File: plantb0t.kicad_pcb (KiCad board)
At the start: 2 copper layers, 50 x 50 mm, 56 parts, among them P1 CONN_02X09, P2 USB_OTG, P3 CONN_02X03, P4 CONN_01X02, P5 CONN_01X02, P6 CONN_01X02, P7 CONN_01X02, P8 CONN_01X04, P9 CONN_01X04, Q1 BS170, Q2 BS170, SW1 SWITCH_INV, U1 ESP-12, U10 BMP280, U11 74HC(T)4051, U12 LEDx2, U2 CP2102, U3 ZXCL5213V30H5CT-ND, U4 MCP4017 100K, U5 FXL6408, U6 FC6946010R, U7 FC6946010R, U8 MCP6001, U9 PSSI2021SAY

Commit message: Starting routing from scratch
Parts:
- added P10: CONN_01X01, Connect:1pin, F.Cu at (70.0, 85.0)
- added P11: CONN_01X01, Connect:1pin, F.Cu at (70.0, 45.0)
- added P12: CONN_01X01, Connect:1pin, F.Cu at (110.0, 85.0)
- added P13: CONN_01X01, Connect:1pin, F.Cu at (110.0, 45.0)
- C1, C4, C6: footprint Capacitors_Tantalum_SMD:TantalC_SizeA_EIA-3216_HandSoldering -> Capacitors_SMD:c_elec_4x5.3
- C10, C11, C12, C13, C7, C8, C9: footprint Capacitors_SMD:C_0603 -> Capacitors_SMD:C_0805
- C2, C3, C5: footprint Capacitors_SMD:C_1206 -> Capacitors_SMD:C_0805
- SW1: footprint Buttons_Switches_ThroughHole:SW_Micro_SPST_Angled -> Buttons_Switches_SMD:SW_SPST_B3U-3100P-B
- moved C1 148.5 mm to (200.9, 104.5), turned to 0 degrees
- moved R6 143.9 mm to (220.8, 89.9)
- moved R4 142.7 mm to (215.6, 91.9), turned to 0 degrees
- moved U5 141.4 mm to (195.5, 150.6)
- moved R8 138.7 mm to (206.1, 109.1), turned to 0 degrees
- moved D1 138.6 mm to (211.6, 95.2), turned to 0 degrees
- moved R10 134.6 mm to (205.3, 138.6), turned to 0 degrees
- moved U8 133.4 mm to (207.3, 126.1)
- moved Q2 130.8 mm to (195.9, 136.5)
- moved D4 130.5 mm to (197.8, 98.6), turned to 0 degrees
- moved C7 124.8 mm to (205.9, 132.6)
- moved U11 123.9 mm to (198.4, 127.1), turned to 0 degrees
- moved Q1 122.6 mm to (192.8, 98.6), turned to 0 degrees
- moved C5 118.5 mm to (190.9, 114.9)
- moved P7 111.4 mm to (188.3, 128.6), turned to 0 degrees
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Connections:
- net /Sensor Mounts/GPIO_1 renamed /GPIO_1
- net /Sensor Mounts/I2C_CLOCK renamed /I2C_CLOCK
- net /Sensor Mounts/I2C_DATA renamed /I2C_DATA
- net /Sensor Mounts/SENSE_WIRE renamed /SENSORS
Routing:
- net /I2C_DATA: track 78.5 -> 0.00 mm, vias 1 -> 0
- net /I2C_CLOCK: track 61.0 -> 0.00 mm, vias 1 -> 0
- net +3V3: track 54.1 -> 0.00 mm, vias 1 -> 0
- net /PERM_3V3: track 88.3 -> 35.5 mm, vias 1 -> 0
- net /ESP_RESET: track 50.9 -> 9.99 mm
- net /GPIO_2: track 40.1 -> 0.00 mm
- net /GPIO_3: track 38.6 -> 0.00 mm
- net /GPIO_4: track 37.3 -> 0.00 mm
- net /CH_PD: track 40.8 -> 10.1 mm
- net /GPIO_6: track 20.8 -> 0.00 mm
- net /GPIO_5: track 20.4 -> 0.00 mm
- net /SLEEP_CTRL: track 19.9 -> 0.00 mm, vias 1 -> 0
- net /GPIO_7: track 18.4 -> 0.00 mm
- net /FLASH_TX: track 41.3 -> 56.7 mm, vias 1 -> 0
- net +5V: track 49.3 -> 60.8 mm, vias 3 -> 0
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
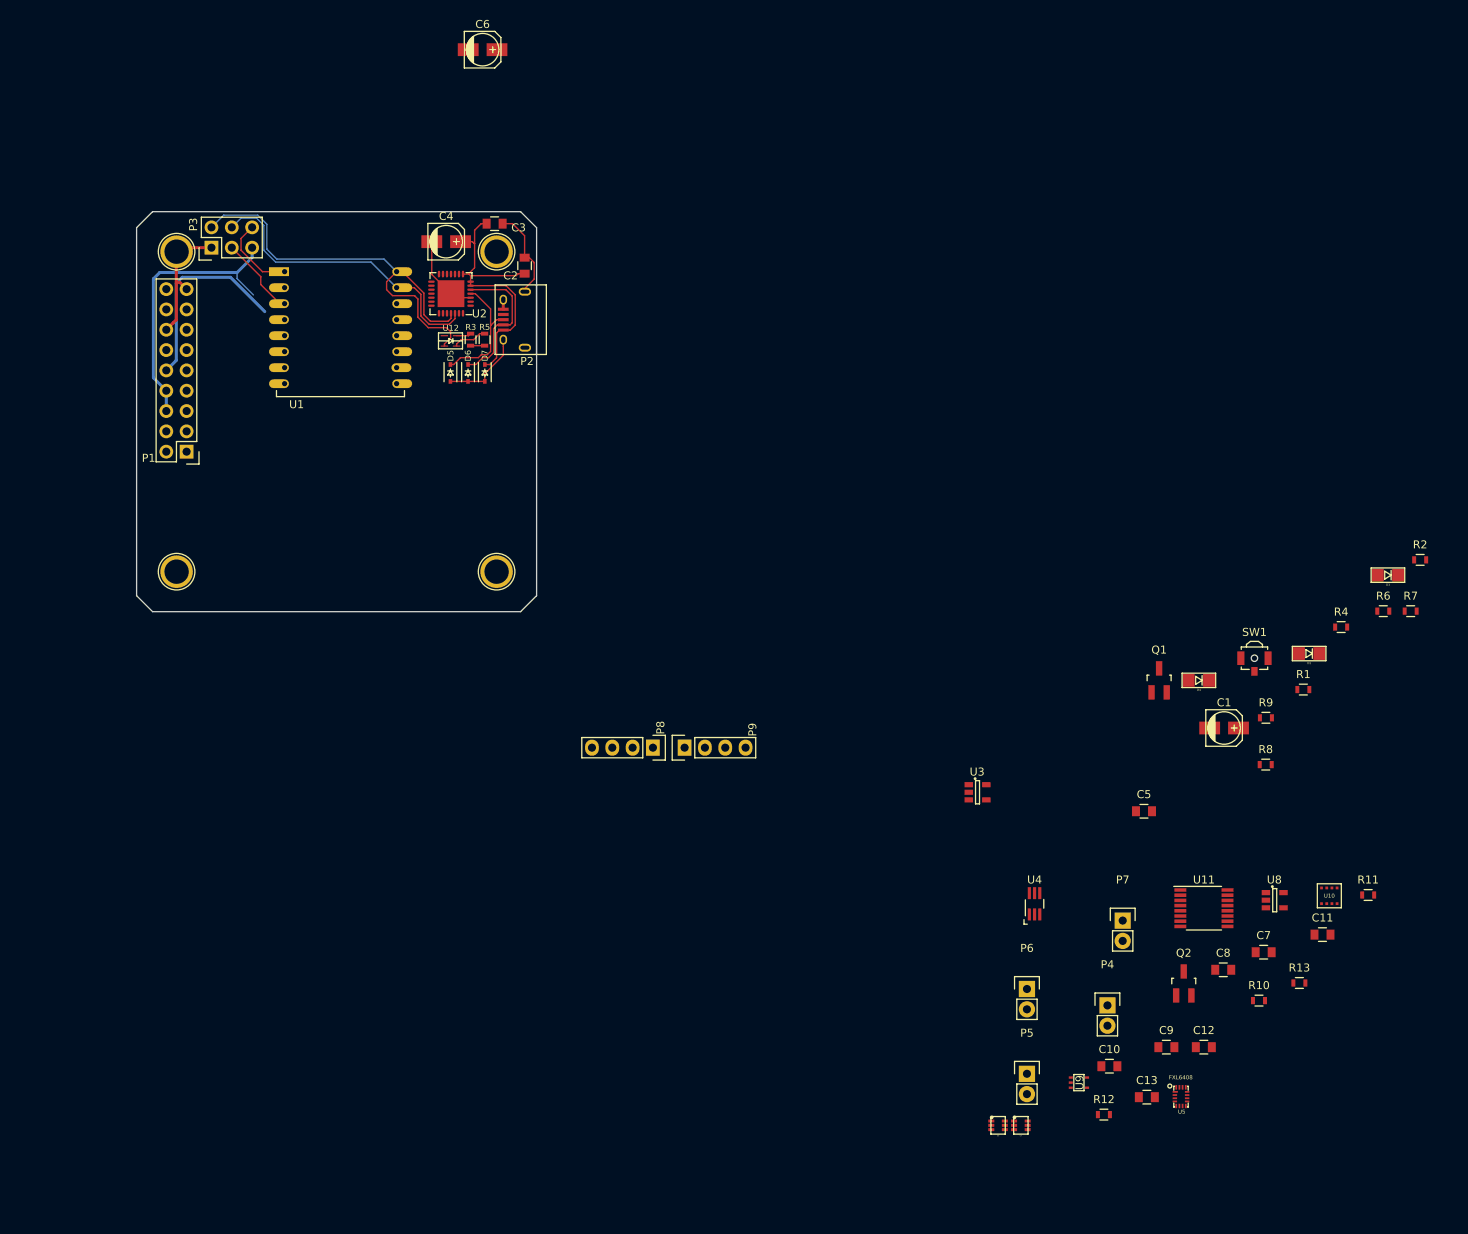
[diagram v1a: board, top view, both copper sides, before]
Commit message: Fiddling with the 5V plane for decoupling around the USB programmer
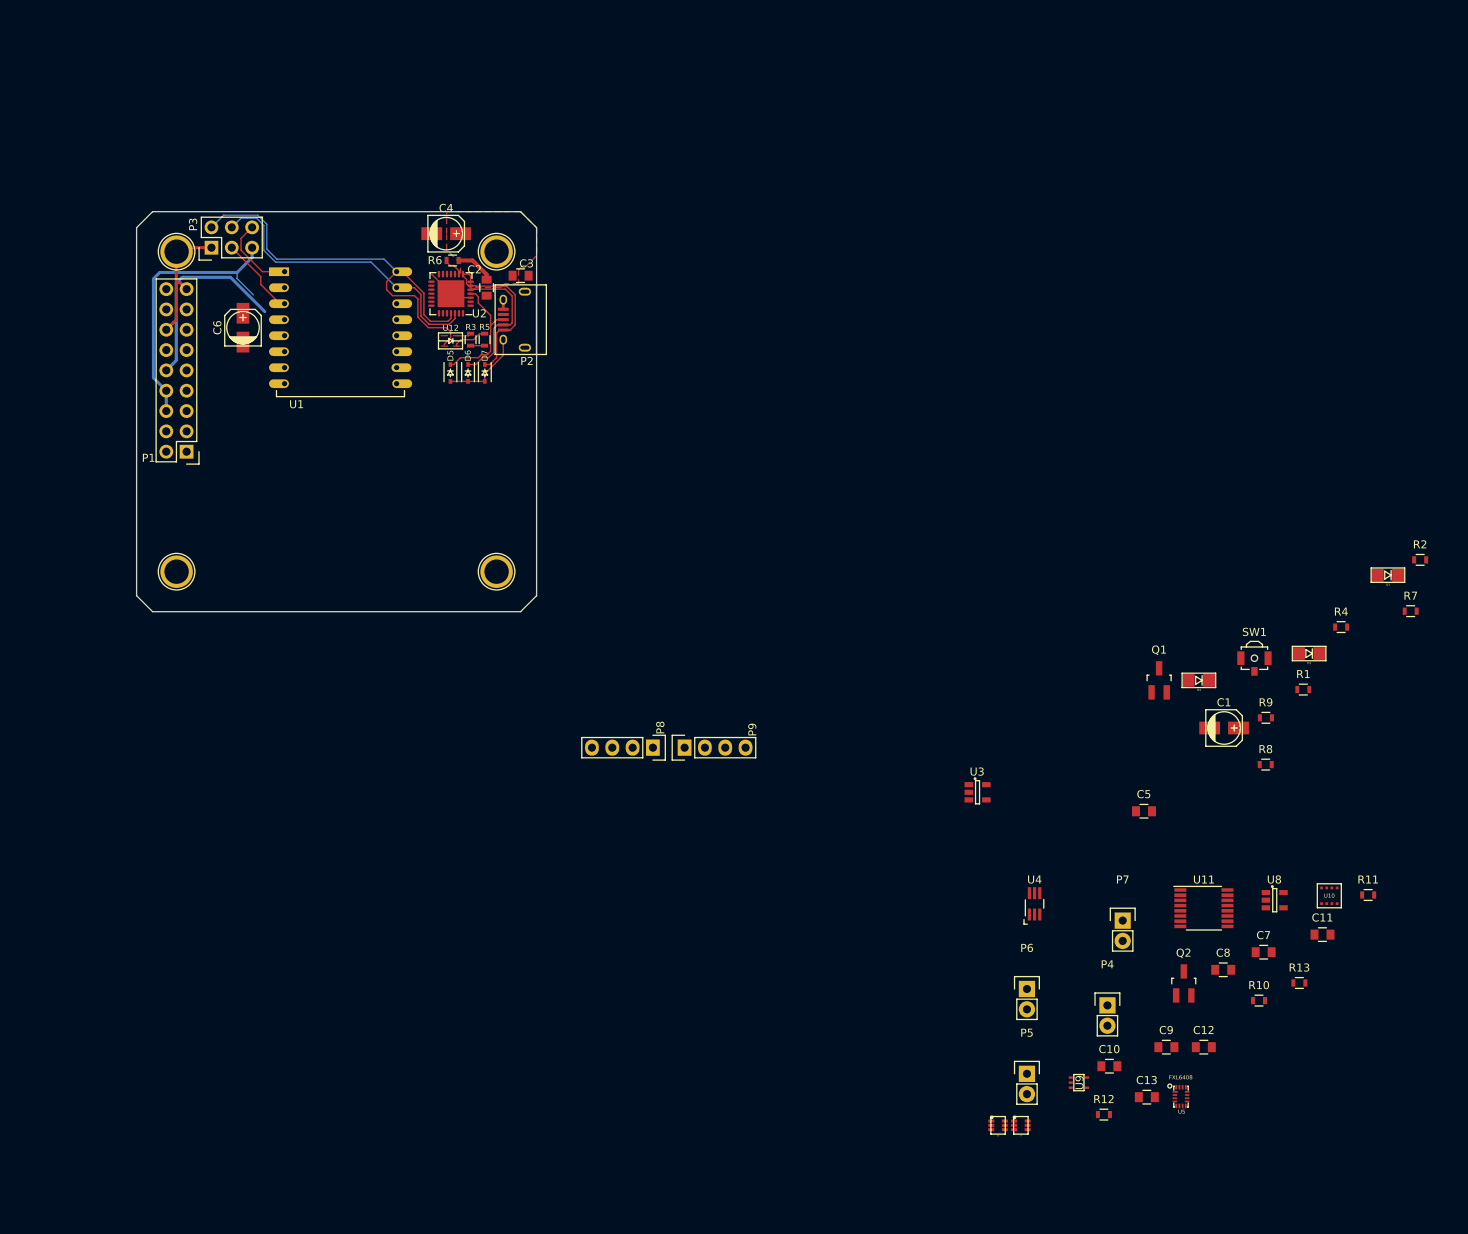
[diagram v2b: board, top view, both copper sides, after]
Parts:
- moved R6 124.3 mm to (104.5, 46.1)
- moved C6 45.9 mm to (78.3, 54.5), turned to 90 degrees
- moved C3 7.27 mm to (113.0, 48.0)
- moved C2 5.49 mm to (108.8, 49.5), turned to 270 degrees
- moved C4 1.00 mm to (103.7, 42.8)
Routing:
- net GND: track 56.6 -> 41.2 mm
- net +5V: track 60.8 -> 49.3 mm
- net Net-(R6-Pad1): track 0.00 -> 2.61 mm
- added copper zone on F.Cu, net +5V

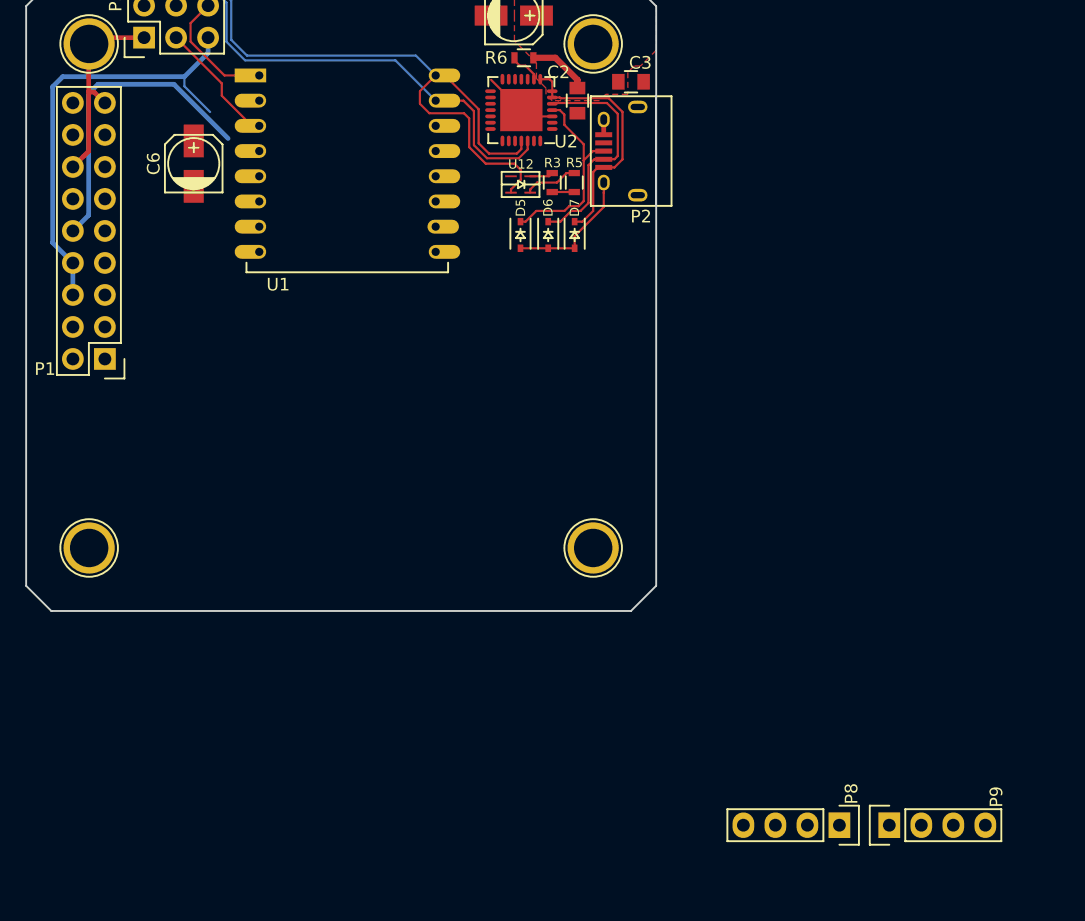
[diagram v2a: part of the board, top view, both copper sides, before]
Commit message: Adding a few GPIO pins to the header and wiring up I²C expander sockets
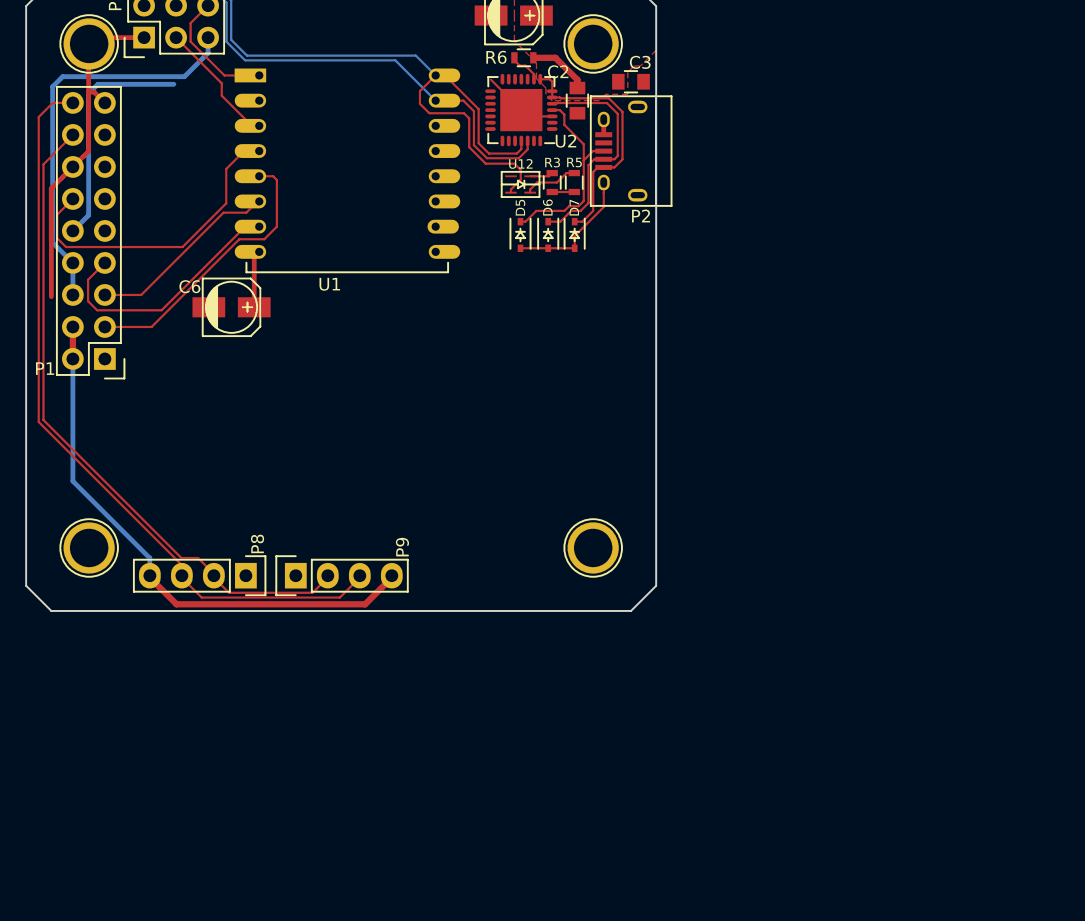
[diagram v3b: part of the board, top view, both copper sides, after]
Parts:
- moved P8 51.1 mm to (82.4, 87.2)
- moved P9 51.1 mm to (86.4, 87.2)
- moved C6 11.8 mm to (81.3, 65.9), turned to 0 degrees
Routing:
- net /I2C_CLOCK: track 0.00 -> 60.0 mm
- net /I2C_DATA: track 0.00 -> 52.7 mm
- net +3V3: track 0.00 -> 43.5 mm
- net /SLEEP_CTRL: track 0.00 -> 24.7 mm
- net /GPIO_2: track 0.00 -> 22.2 mm
- net /GPIO_4: track 0.00 -> 20.2 mm
- net /GPIO_3: track 0.00 -> 15.3 mm
- net GND: track 41.2 -> 53.1 mm
- net +5V: track 49.3 -> 43.3 mm
- net /PERM_3V3: track 35.5 -> 36.4 mm
